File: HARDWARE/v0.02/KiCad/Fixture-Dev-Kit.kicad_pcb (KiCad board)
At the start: 2 copper layers, 145 x 126.3 mm, 174 parts, among them J1 DUT, J10 LED_3, J11 FET_0, J12 FET_0, J13 NFET_0, J14 NFET_1, J15 Conn_01x20, J16 Conn_01x20, J17 CHIP4RH, J18 SW_0, J19 SW_0, J2 POWER, J20 Conn_01x20, J21 Conn_01x20, J22 SW_0, J23 CHIP4LH, J24 SW_0, J25 JST-2P-RA, J26 SW_0, J27 INA_40, J28 INA_40, J29 INA_40, J3 LED_0, J30 INA_40, J31 ADS, J32 SW_0, J33 SW_0, J34 SW_0, J35 40 V+, J36 41 V+, J37 42 V+, J38 43 V+, J39 DUT BAT, J4 LED_1, J40 DUT BAT, J5 LED_2, J6 LED_3, J7 LED_0, J8 LED_1, J9 LED_2, Q1 NTF2955T1G, Q10 NTF2955-D, Q11 NTF2955-D, Q12 NTF2955-D, Q13 FDN337N, Q14 FDN337N, Q15 FDN337N, Q16 FDN337N, Q2 NTF2955T1G, Q3 FDN337N, Q4 FDN337N, Q5 NTF2955-D, Q6 NTF2955-D, Q7 NTF2955-D, Q8 NTF2955-D, Q9 NTF2955-D, SW1 TL9210AF260Q, SW2 TL9210AF260Q, SW3 TL9210AF260Q, SW4 TL9210AF260Q, SW5 YSS-19-1202-N, SW6 TL9210AF260Q, U1 INA219BIDCNT, U2 INA219BIDCNT, U3 INA219BIDCNT, U4 INA219BIDCNT, U5 ADS1015IDGST

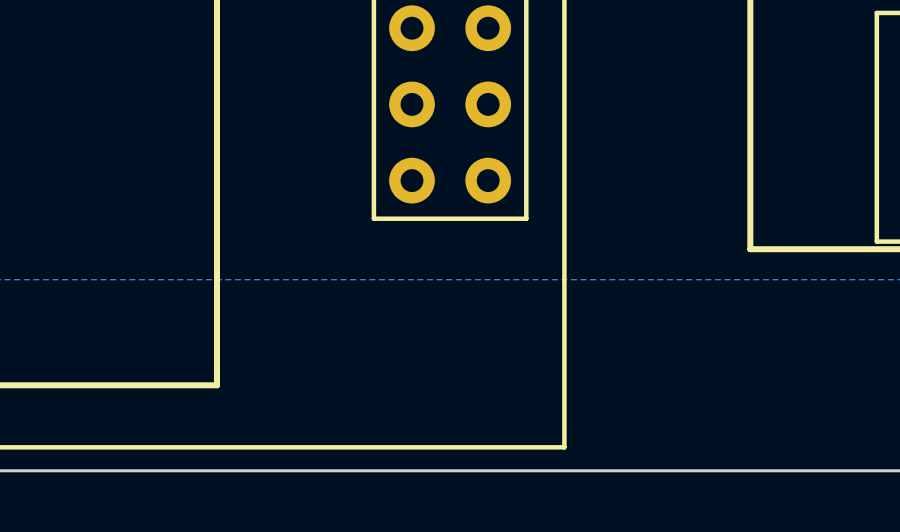
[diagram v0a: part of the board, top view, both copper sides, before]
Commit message: adding 3v3 line up to DUT header
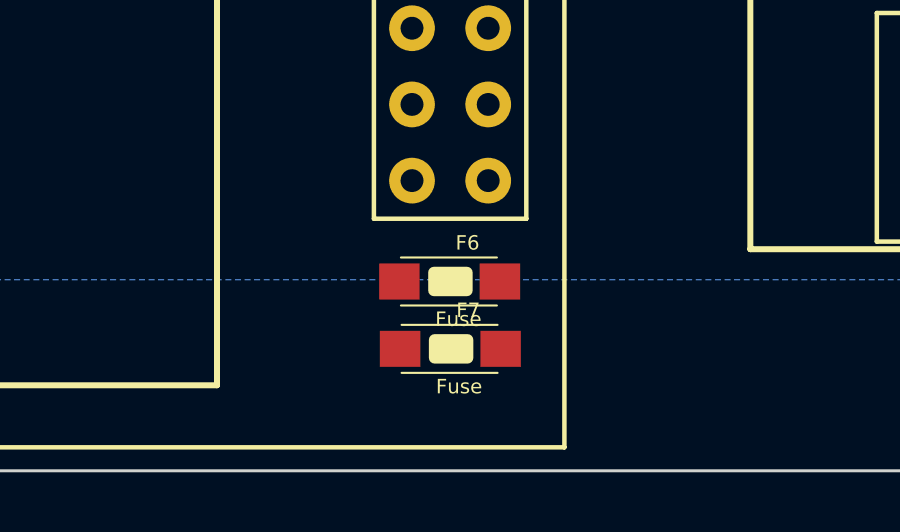
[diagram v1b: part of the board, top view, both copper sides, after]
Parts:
- added F6: Fuse, 1206:1206, F.Cu at (73.1, 140.0)
- added F7: Fuse, 1206:1206, F.Cu at (73.1, 142.3)
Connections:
- J1 pad 2: GND -> Net-(F6-Pad2)
- J1 pad 4: GND -> Net-(F7-Pad2)
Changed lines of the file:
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@@
 (kicad_pcb (version 4) (host pcbnew 4.0.7-e2-6376~58~ubuntu17.04.1)
   (general
-    (links 398)
-    (no_connects 19)
-    (area 24.949999 19.949999 170.050001 140.050001)
+    (links 400)
+    (no_connects 22)
+    (area 24.949999 19.949999 170.062001 146.374001)
     (thickness 1.6)
     (drawings 73)
     (tracks 1308)
     (zones 0)
-    (modules 174)
-    (nets 183)
+    (modules 176)
+    (nets 185)
   )
   (page A4)
@@
   (net 181 "Net-(J39-Pad1)")
   (net 182 "Net-(J39-Pad2)")
+  (net 183 "Net-(F6-Pad2)")
+  (net 184 "Net-(F7-Pad2)")
   (net_class Default "This is the default net class."
     (clearance 0.2)
@@
     (add_net "Net-(F5-Pad1)")
     (add_net "Net-(F5-Pad2)")
+    (add_net "Net-(F6-Pad2)")
+    (add_net "Net-(F7-Pad2)")
     (add_net "Net-(J10-Pad1)")
     (add_net "Net-(J15-Pad10)")
@@
       (net 46 /AIN3))
     (pad 2 thru_hole circle (at 11.43 -24.13 270) (size 1.524 1.524) (drill 0.762) (layers *.Cu *.Mask)
-      (net 2 GND))
+      (net 183 "Net-(F6-Pad2)"))
     (pad 3 thru_hole circle (at 8.89 -26.67 270) (size 1.524 1.524) (drill 0.762) (layers *.Cu *.Mask)
       (net 45 /AIN2))
     (pad 4 thru_hole circle (at 8.89 -24.13 270) (size 1.524 1.524) (drill 0.762) (layers *.Cu *.Mask)
-      (net 2 GND))
+      (net 184 "Net-(F7-Pad2)"))
     (pad 5 thru_hole circle (at 6.35 -26.67 270) (size 1.524 1.524) (drill 0.762) (layers *.Cu *.Mask)
       (net 44 /AIN1))
@@
       (net 2 GND))
   )
+  (module 1206:1206 (layer F.Cu)
+    (at 73.112 140.014 180)
+    (descr "Multilayer SMD")
+    (attr smd)
+    (fp_text reference F6 (at -0.62201 1.2852 180) (layer F.SilkS)
+      (effects (font (size 0.480936 0.480936) (thickness 0.05)))
+    )
+    (fp_text value Fuse (at -0.31649 -1.25925 180) (layer F.SilkS)
+      (effects (font (size 0.480745 0.480745) (thickness 0.05)))
+    )
+    (fp_line (start -1.7 0) (end 1.7 0) (layer Dwgs.User) (width 0.127))
+    (fp_line (start -1.6 -0.8) (end 1.6 -0.8) (layer F.SilkS) (width 0.07))
+    (fp_line (start 1.6 -0.8) (end 1.6 0.8) (layer Dwgs.User) (width 0.07))
+    (fp_line (start 1.6 0.8) (end -1.6 0.8) (layer F.SilkS) (width 0.07))
+    (fp_line (start -1.6 0.8) (end -1.6 -0.8) (layer Dwgs.User) (width 0.07))
+    (fp_poly (pts (xy -0.600858 -0.3) (xy 0.5 -0.3) (xy 0.5 0.300429) (xy -0.600858 0.300429)) (layer F.SilkS) (width 0.381))
+    (pad 1 smd rect (at -1.7 0 180) (size 1.35 1.2) (layers F.Cu F.Paste F.Mask)
+      (net 8 +5V))
+    (pad 2 smd rect (at 1.65 0 180) (size 1.35 1.2) (layers F.Cu F.Paste F.Mask)
+      (net 183 "Net-(F6-Pad2)"))
+  )
+  (module 1206:1206 (layer F.Cu)
+    (at 73.135 142.26 180)
+    (descr "Multilayer SMD")
+    (attr smd)
+    (fp_text reference F7 (at -0.62201 1.2852 180) (layer F.SilkS)
+      (effects (font (size 0.480936 0.480936) (thickness 0.05)))
+    )
+    (fp_text value Fuse (at -0.31649 -1.25925 180) (layer F.SilkS)
+      (effects (font (size 0.480745 0.480745) (thickness 0.05)))
+    )
+    (fp_line (start -1.7 0) (end 1.7 0) (layer Dwgs.User) (width 0.127))
+    (fp_line (start -1.6 -0.8) (end 1.6 -0.8) (layer F.SilkS) (width 0.07))
+    (fp_line (start 1.6 -0.8) (end 1.6 0.8) (layer Dwgs.User) (width 0.07))
+    (fp_line (start 1.6 0.8) (end -1.6 0.8) (layer F.SilkS) (width 0.07))
+    (fp_line (start -1.6 0.8) (end -1.6 -0.8) (layer Dwgs.User) (width 0.07))
+    (fp_poly (pts (xy -0.600858 -0.3) (xy 0.5 -0.3) (xy 0.5 0.300429) (xy -0.600858 0.300429)) (layer F.SilkS) (width 0.381))
+    (pad 1 smd rect (at -1.7 0 180) (size 1.35 1.2) (layers F.Cu F.Paste F.Mask)
+      (net 21 /C4-VCC-3V3))
+    (pad 2 smd rect (at 1.65 0 180) (size 1.35 1.2) (layers F.Cu F.Paste F.Mask)
+      (net 184 "Net-(F7-Pad2)"))
+  )
   (gr_line (start 65.382 107.024) (end 32.362 107.024) (angle 90) (layer F.SilkS) (width 0.2))
   (gr_line (start 65.382 143.474) (end 65.382 107.024) (angle 90) (layer F.SilkS) (width 0.2))
@@
   (segment (start 69.85 44.196) (end 69.85 51.816) (width 0.254) (layer B.Cu) (net 1))
   (segment (start 69.85 51.816) (end 71.12 53.086) (width 0.254) (layer B.Cu) (net 1) (status 20))
-  (segment (start 73.662 83.484) (end 73.662 83.568) (width 1) (layer F.Cu) (net 2) (status C00000))
-  (segment (start 73.662 83.568) (end 76.2 86.106) (width 1) (layer F.Cu) (net 2) (status C00000))
+  (segment (start 73.662 83.484) (end 73.662 83.568) (width 1) (layer F.Cu) (net 2))
+  (segment (start 73.662 83.568) (end 76.2 86.106) (width 1) (layer F.Cu) (net 2))
   (segment (start 99.6696 90.7034) (end 100.3554 90.7034) (width 1) (layer F.Cu) (net 2) (status 30))
   (segment (start 100.3554 90.7034) (end 101.854 92.202) (width 1) (layer F.Cu) (net 2) (status 10))
@@
   (segment (start 67.31 89.916) (end 67.31 97.536) (width 0.254) (layer B.Cu) (net 99))
   (segment (start 67.31 97.536) (end 68.58 98.806) (width 0.254) (layer B.Cu) (net 99) (status 20))
-  (segment (start 71.12 88.646) (end 71.12 88.642) (width 0.25) (layer F.Cu) (net 100) (status C00000))
-  (segment (start 71.12 88.642) (end 69.892 87.414) (width 0.25) (layer F.Cu) (net 100) (status 400000))
-  (segment (start 69.892 84.554) (end 70.962 83.484) (width 0.25) (layer F.Cu) (net 100) (status 800000))
+  (segment (start 71.12 88.646) (end 71.12 88.642) (width 0.25) (layer F.Cu) (net 100))
+  (segment (start 71.12 88.642) (end 69.892 87.414) (width 0.25) (layer F.Cu) (net 100))
+  (segment (start 69.892 84.554) (end 70.962 83.484) (width 0.25) (layer F.Cu) (net 100))
   (segment (start 69.892 87.414) (end 69.892 84.554) (width 0.25) (layer F.Cu) (net 100))
   (segment (start 71.12 88.646) (end 71.12 93.472) (width 0.25) (layer B.Cu) (net 100) (status 10))

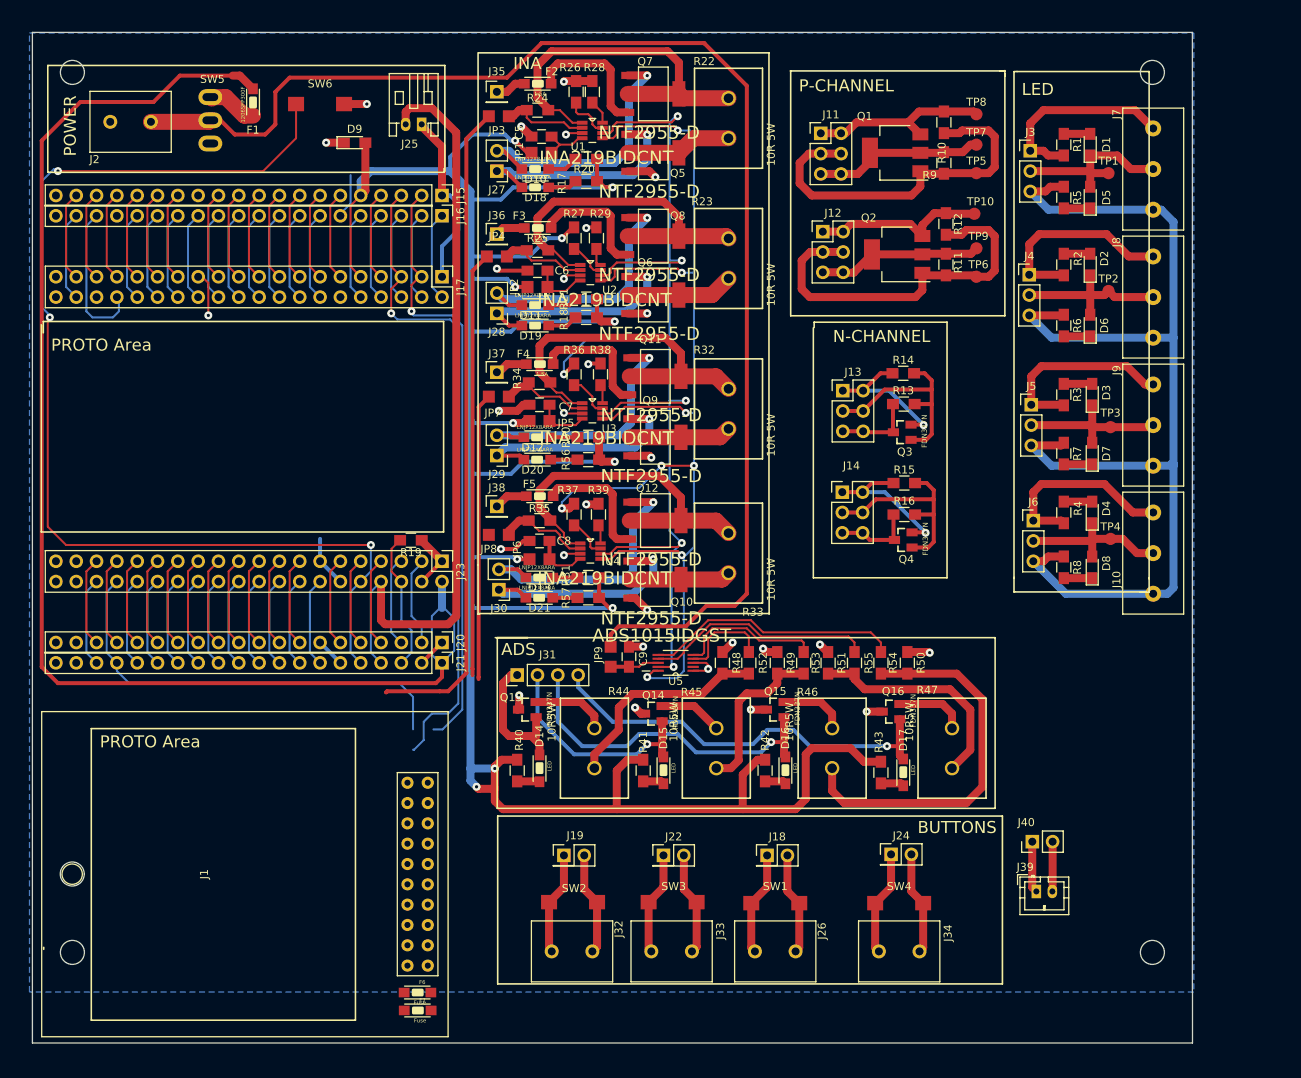
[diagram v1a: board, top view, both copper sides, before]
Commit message: adding latest updates from pcb layout designed 11/8/2017
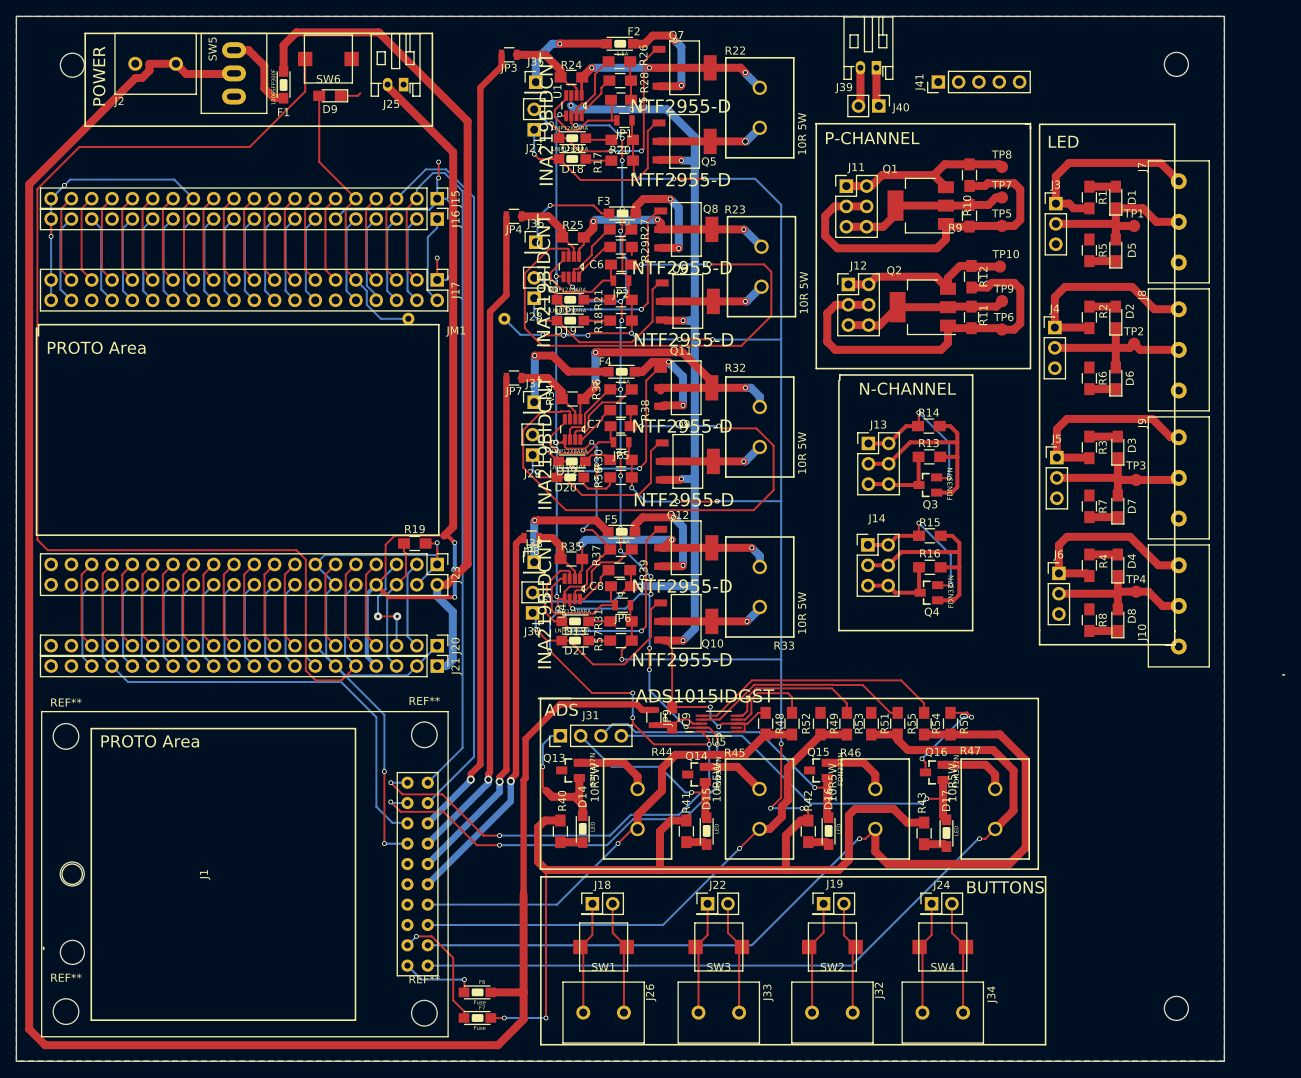
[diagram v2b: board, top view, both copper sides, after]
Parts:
- added J41: Conn_01x05, Pin_Headers:Pin_Header_Straight_1x05_Pitch2.54mm, F.Cu at (138.2, 26.2)
- added JM1: JUMPER, Jumper:Jumper, F.Cu at (78.0, 55.8)
- added REF**: MountingHole_3.2mm_M3, Mounting_Holes:MountingHole_3.2mm_M3, F.Cu at (29.2, 108.0)
- added REF**: MountingHole_3.2mm_M3, Mounting_Holes:MountingHole_3.2mm_M3, F.Cu at (29.2, 142.4)
- added REF**: MountingHole_3.2mm_M3, Mounting_Holes:MountingHole_3.2mm_M3, F.Cu at (74.0, 142.6)
- added REF**: MountingHole_3.2mm_M3, Mounting_Holes:MountingHole_3.2mm_M3, F.Cu at (74.0, 107.8)
- J39: footprint Connectors_JST:JST_PH_B2B-PH-K_02x2.00mm_Straight -> Connectors_JST:JST_PH_S2B-PH-K_02x2.00mm_Angled
- JP1, JP2, JP3, JP4, JP5, JP6, JP7, JP8, JP9: footprint ConnectedCutJumper:connectedCutJumper -> Resistors_SMD:R_0805
- moved J39 104.9 mm to (130.5, 24.4), turned to 180 degrees
- moved J40 93.9 mm to (130.8, 29.2), turned to 270 degrees
- moved J32 33.4 mm to (125.0, 142.5)
- moved J19 33.0 mm to (123.9, 128.9)
- moved SW2 32.9 mm to (125.0, 134.3)
- moved J26 22.8 mm to (96.4, 142.5)
- moved J18 22.7 mm to (95.0, 128.9)
- moved SW1 22.1 mm to (96.4, 134.3)
- moved JP6 11.9 mm to (98.8, 91.6), turned to 180 degrees
- moved C8 11.6 mm to (98.6, 89.2), turned to 180 degrees
- moved F2 11.4 mm to (98.4, 21.4)
- moved F5 11.2 mm to (98.6, 82.4)
- moved JP1 11.1 mm to (99.0, 31.0), turned to 180 degrees
- moved C5 10.9 mm to (98.6, 28.4), turned to 180 degrees
- moved F3 10.7 mm to (98.7, 42.6)
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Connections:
- D9 pad 2: /C4-VCC-3V3 -> /Fixture Dev Kit - Functional Computer/STATUSLED
- J15 pad 5: /C4-VCC-3V3 -> /Fixture Dev Kit - Functional Computer/STATUSLED
- J16 pad 17: (no net) -> Net-(J16-Pad17)
- J17 pad 9: /C4-VCC-3V3 -> /Fixture Dev Kit - Functional Computer/STATUSLED
- SW5 pad 1: (no net) -> Net-(SW5-Pad1)
- U5 pad 2: (no net) -> Net-(U5-Pad2)
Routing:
- net GND: track 264.2 -> 488.9 mm, vias 29 -> 26
- net +5V: track 168.8 -> 260.6 mm
- net /AIN3: track 28.3 -> 106.3 mm, vias 0 -> 1
- net /Fixture Dev Kit - Functional Computer/C4-PWR-IN: track 175.6 -> 104.2 mm
- net /AIN2: track 48.1 -> 110.0 mm, vias 0 -> 1
- net /INA43_V-: track 0.23 -> 48.1 mm, vias 0 -> 1
- net /AIN1: track 20.8 -> 65.5 mm, vias 0 -> 1
- net /I2C-SCK: track 144.7 -> 184.2 mm, vias 8 -> 15
- net /I2C-SDA: track 137.5 -> 175.9 mm, vias 6 -> 22
- net /Fixture Dev Kit - Functional Computer/STATUSLED: track 0.00 -> 35.6 mm
- net /AIN0: track 26.9 -> 57.0 mm, vias 0 -> 1
- net /INA41_V-: track 53.1 -> 82.5 mm, vias 0 -> 1
- net /INA42_V-: track 35.8 -> 64.8 mm, vias 0 -> 1
- net /C4-VCC-3V3: track 340.3 -> 316.7 mm, vias 11 -> 18
- net /UART-RX: track 81.8 -> 102.2 mm, vias 1 -> 0
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- added copper zone on B.Cu, net +5V
- added copper zone on F.Cu, net GND
- removed copper zone on B.Cu, net GND
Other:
- board size 145 x 126.3 mm -> 151 x 130.6 mm
- net class C4-PWR-IN​ added: clearance 0.4, trace_width 1.4, via_dia 1, via_drill 0.6
- net class INA added: clearance 0.4, trace_width 0.8, via_dia 1, via_drill 0.6
- net class Misc added: clearance 0.2, trace_width 0.25, via_dia 2, via_drill 1
- board text removed: "INA"
